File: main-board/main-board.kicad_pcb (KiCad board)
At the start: 2 copper layers, 62 parts, among them J1 MOTOR0, J10 PROGRAMMER, J11 CAM0, J12 CAM1, J13 CAM2, J14 CAM3, J15 CAM4, J16 CAM5, J17 CAM6, J18 CAM7, J19 PowerBoard Interface, J2 MOTOR1, J20 IMU Breakout, J21 ICSP (DO NOT POPULATE), J3 MOTOR2, J4 MOTOR3, J5 RJ45, J6 MOTOR4, J7 MOTOR5, J8 MOTOR6, J9 MOTOR7, SW1 SW_SPST, T1 ATB2012E-50011M-T01, T2 ATB2012E-50011M-T01, U1 MCP2515-EST, U2 ATA6560, U3 ATmega2560-16AU | Main Proc, U4 MC14051B, U5 MC14051B, U6 SN75HVD3082EDR, U7 LTC1983ES6-5-TRPBF, U8 OPAMP, U9 OPAMP, Y1 20MHz, Y2 20MHz

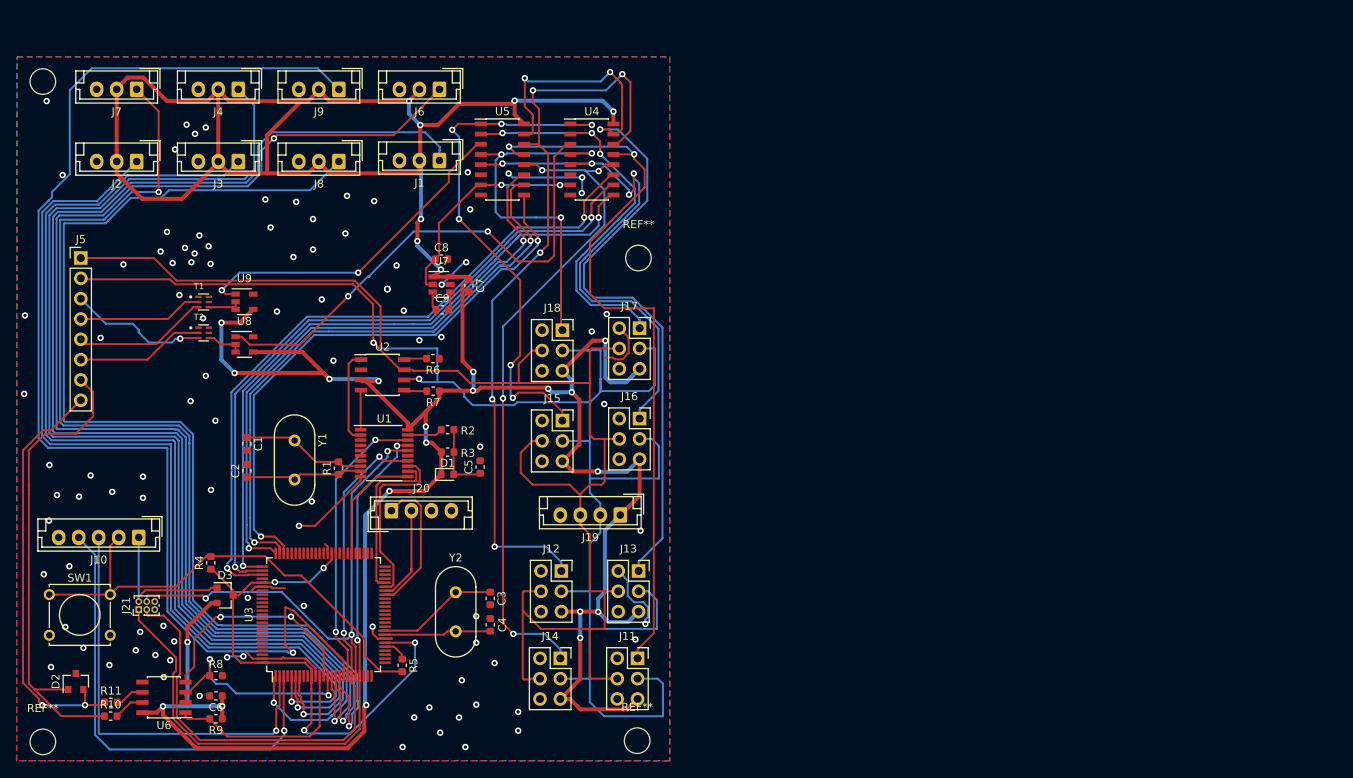
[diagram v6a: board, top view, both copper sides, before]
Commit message: Various changes (see description)
Schematic Changes:
* add optional second RS485
* add filter caps to IC power
* remove input resistor on reset line of 2560
* change CAN UART lines to be tx<>tx rx<>rx

PCB Changes:
* reorganize camera section
* add header labels
* minor fixes
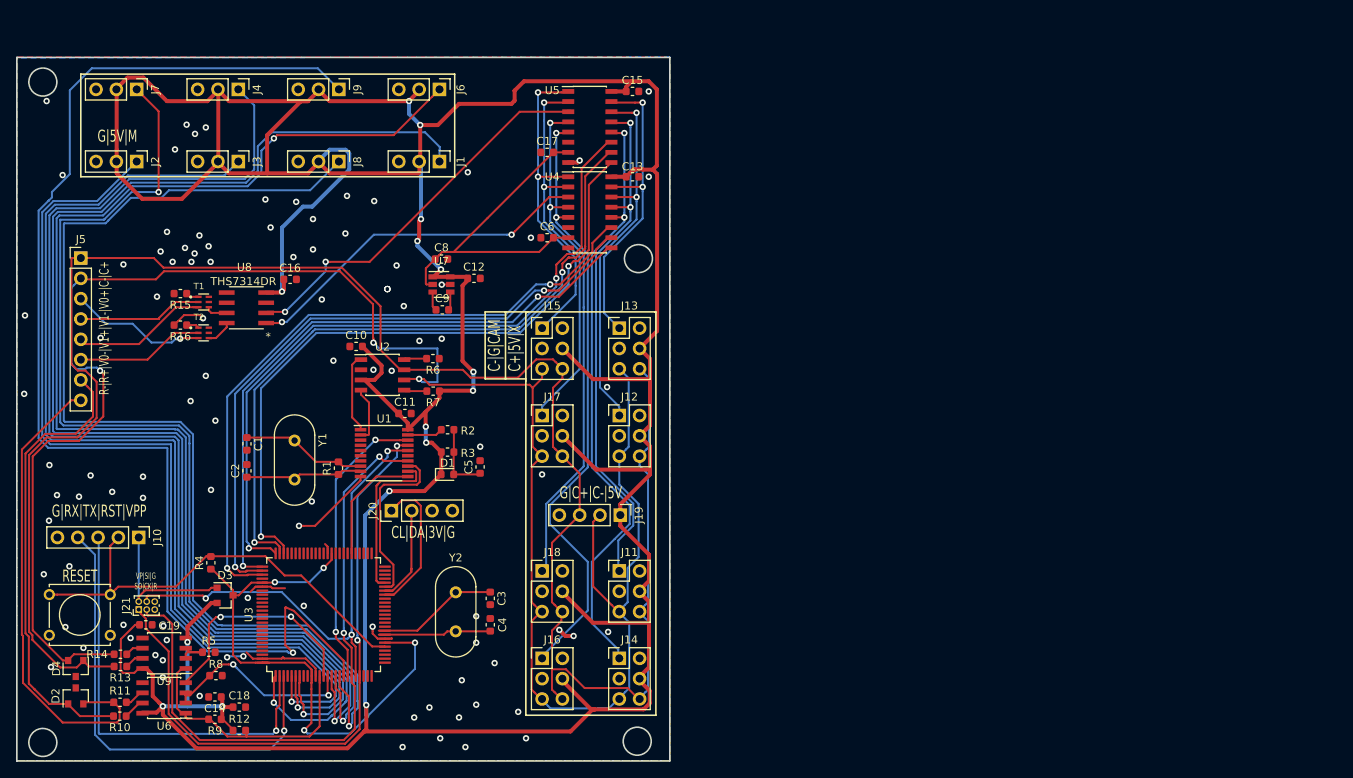
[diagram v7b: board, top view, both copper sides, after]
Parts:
- removed C7: 10uF, Capacitor_SMD:C_0603_1608Metric
- removed REF** (x4): MountingHole_3.2mm_M3, MountingHole:MountingHole_3.2mm_M3
- added C10: 100nF, Capacitor_SMD:C_0603_1608Metric, F.Cu at (107.4, 77.5)
- added C11: 100nF, Capacitor_SMD:C_0603_1608Metric, F.Cu at (113.5, 85.9)
- added C12: 100nF, Capacitor_SMD:C_0603_1608Metric, F.Cu at (122.2, 69.0)
- added C13: 100nF, Capacitor_SMD:C_0603_1608Metric, F.Cu at (142.0, 56.3)
- added C14: 100nF, Capacitor_SMD:C_0603_1608Metric, F.Cu at (89.8, 121.3)
- added C15: 100nF, Capacitor_SMD:C_0603_1608Metric, F.Cu at (142.0, 45.6)
- added C16: 100nF, Capacitor_SMD:C_0603_1608Metric, F.Cu at (99.2, 69.1)
- added C17: 100nF, Capacitor_SMD:C_0603_1608Metric, F.Cu at (131.3, 53.2)
- added C18: 100nF, Capacitor_SMD:C_0603_1608Metric, F.Cu at (92.8, 122.6)
- added C19: 100nF, Capacitor_SMD:C_0603_1608Metric, F.Cu at (81.2, 112.3)
- added D4: CDSOT23-SM712, Package_TO_SOT_SMD:SOT-23, F.Cu at (72.4, 117.7)
- added R12: 10k, Resistor_SMD:R_0603_1608Metric, F.Cu at (92.8, 125.5)
- added R13: 10, Resistor_SMD:R_0603_1608Metric, F.Cu at (78.0, 117.5)
- added R14: 10, Resistor_SMD:R_0603_1608Metric, F.Cu at (78.0, 116.0)
- added R15: 100, Resistor_SMD:R_0603_1608Metric, F.Cu at (85.5, 70.9)
- added R16: 100, Resistor_SMD:R_0603_1608Metric, F.Cu at (85.5, 74.8)
- J1, J2, J3, J4, J6, J7, J8, J9: footprint Connector_JST:JST_EH_B03B-EH-A_1x03_P2.50mm_Vertical -> Connector_PinHeader_2.54mm:PinHeader_1x03_P2.54mm_Vertical
- J10: footprint Connector_JST:JST_EH_B05B-EH-A_1x05_P2.50mm_Vertical -> Connector_PinHeader_2.54mm:PinHeader_1x05_P2.54mm_Vertical
- J11, J12, J13, J14, J15, J16, J17, J18: footprint Connector_PinSocket_2.54mm:PinSocket_2x03_P2.54mm_Vertical -> Connector_PinHeader_2.54mm:PinHeader_2x03_P2.54mm_Vertical
- J19, J20: footprint Connector_JST:JST_EH_B04B-EH-A_1x04_P2.50mm_Vertical -> Connector_PinHeader_2.54mm:PinHeader_1x04_P2.54mm_Vertical
- R5: value 100k -> 10k
- U8: value OPAMP -> THS7314DR; footprint Package_TO_SOT_SMD:SOT-23-5 -> ths7314dr:THS7314DR
- U9: value OPAMP -> SN75HVD3082EDR; footprint Package_TO_SOT_SMD:SOT-23-5 -> Package_SO:SOIC-8_3.9x4.9mm_P1.27mm
- moved C6 70.7 mm to (131.3, 63.9)
- moved U9 45.1 mm to (83.4, 115.8), turned to 180 degrees
- moved J16 32.4 mm to (130.7, 116.5)
- moved J13 30.4 mm to (140.3, 75.2)
- moved J18 30.2 mm to (130.7, 105.5)
- moved R5 24.2 mm to (89.0, 115.7), turned to 0 degrees
- moved J12 20.7 mm to (140.3, 86.1)
- moved J17 16.4 mm to (130.7, 86.1)
- moved J15 11.8 mm to (130.7, 75.2)
- moved U5 11.7 mm to (136.7, 50.0)
- moved J11 11.2 mm to (140.3, 105.5)
- moved J14 7.37 mm to (140.3, 116.5)
- moved U4 6.61 mm to (136.7, 60.7)
- moved U8 4.58 mm to (93.7, 72.6), turned to 180 degrees
- moved D2 1.81 mm to (72.4, 121.2)
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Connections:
- C6 pad 1: +5V -> -5V
- D3 pad 3: Net-(D3-Pad3) -> +5V
- J11 pad 2: GND -> Net-(J11-Pad2)
- J11 pad 3: CAN- -> GND
- J11 pad 4: CAN+ -> +5V
- J11 pad 5: +5V -> CAN-
- J11 pad 6: Net-(J11-Pad6) -> CAN+
- J12 pad 2: GND -> Net-(J12-Pad2)
- J12 pad 3: CAN- -> GND
- J12 pad 4: CAN+ -> +5V
- J12 pad 5: +5V -> CAN-
- J12 pad 6: Net-(J12-Pad6) -> CAN+
- J13 pad 2: GND -> Net-(J13-Pad2)
- J13 pad 3: CAN- -> GND
- J13 pad 4: CAN+ -> +5V
- J13 pad 5: +5V -> CAN-
- J13 pad 6: Net-(J13-Pad6) -> CAN+
- J14 pad 2: GND -> Net-(J14-Pad2)
- J14 pad 3: CAN- -> GND
- J14 pad 4: CAN+ -> +5V
- J14 pad 5: +5V -> CAN-
- J14 pad 6: Net-(J14-Pad6) -> CAN+
- J15 pad 2: GND -> Net-(J15-Pad2)
- J15 pad 3: CAN- -> GND
- J15 pad 4: CAN+ -> +5V
- J15 pad 5: +5V -> CAN-
- J15 pad 6: Net-(J15-Pad6) -> CAN+
- J16 pad 2: GND -> Net-(J16-Pad2)
- J16 pad 3: CAN- -> GND
- J16 pad 4: CAN+ -> +5V
- J16 pad 5: +5V -> CAN-
- J16 pad 6: Net-(J16-Pad6) -> CAN+
- J17 pad 2: GND -> Net-(J17-Pad2)
- J17 pad 3: CAN- -> GND
- J17 pad 4: CAN+ -> +5V
- J17 pad 5: +5V -> CAN-
- J17 pad 6: Net-(J17-Pad6) -> CAN+
- J18 pad 2: GND -> Net-(J18-Pad2)
- J18 pad 3: CAN- -> GND
- J18 pad 4: CAN+ -> +5V
- J18 pad 5: +5V -> CAN-
- J18 pad 6: Net-(J18-Pad6) -> CAN+
- R4 pad 1: Net-(D3-Pad3) -> +5V
- R5 pad 2: RESET-MAIN -> GND
- T1 pad 1: GND -> Net-(R15-Pad1)
- T2 pad 1: GND -> Net-(R16-Pad1)
- U2 pad 1: Net-(U1-Pad2) -> Net-(U1-Pad1)
- U2 pad 4: Net-(U1-Pad1) -> Net-(U1-Pad2)
- U3 pad 10: Net-(D3-Pad3) -> +5V
- U3 pad 100: Net-(D3-Pad3) -> +5V
- U3 pad 30: Net-(R5-Pad1) -> RESET-MAIN
- U3 pad 31: Net-(D3-Pad3) -> +5V
- U3 pad 61: Net-(D3-Pad3) -> +5V
- U3 pad 80: Net-(D3-Pad3) -> +5V
- U8 pad 2: Net-(T2-Pad4) -> VID-CAM1
- U8 pad 3: Net-(T2-Pad4) -> Net-(U8-Pad3)
- U9 pad 1: VID-CAM1 -> RS485-R
- U9 pad 2: Net-(T1-Pad4) -> Net-(R5-Pad1)
- U9 pad 3: Net-(T1-Pad4) -> Net-(R5-Pad1)
- U9 pad 4: +5V -> Net-(U9-Pad4)
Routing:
- net +5V: track 469.8 -> 624.8 mm, vias 27 -> 19
- net Net-(D3-Pad3): track 71.2 -> 0.00 mm, vias 4 -> 0
- net CAN+: track 178.2 -> 242.6 mm
- net CAM2: track 101.1 -> 38.8 mm, vias 3 -> 2
- net CAN-: track 204.4 -> 255.1 mm, vias 2 -> 3
- net CAM1: track 95.3 -> 47.0 mm, vias 5 -> 2
- net CAM0: track 95.1 -> 65.3 mm
- net CAM4: track 66.8 -> 40.8 mm, vias 6 -> 2
- net GND: track 67.7 -> 43.6 mm, vias 100 -> 98
- net VID-CAM0: track 63.0 -> 44.3 mm
- net CAM7: track 46.8 -> 64.8 mm, vias 3 -> 2
- net -5V: track 28.0 -> 42.1 mm, vias 2 -> 0
- net VID1-0: track 76.8 -> 89.1 mm
- net VID1-2: track 72.7 -> 84.4 mm
- net VID1-1: track 76.2 -> 87.3 mm
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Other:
- board outline added: 81.6 x 87.9 mm
- board text added: "C+|5V|X"
- board text added: "C-|G|CAM"
- board text added: "CL|DA|3V|G"
- board text added: "G|5V|M"
- board text added: "G|C+|C-|5V"
- board text added: "G|RX|TX|RST|VPP"
- board text added: "MISSOURI S&T UNDERWATER ROBOTICS TEAM MAIN BOARD | PCB 1.0.0 | SCH 1.0.0 MATTHEW (COOPER) HEALY, MICHAELA DICKERSON"
- board text added: "R-|R+|V0-|V1+|V1-|V0+|C-|C+"
- board text added: "RESET"
- board text added: "VP|SI|G SO|CK|R"

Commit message: S1.0.1 B1.0.1 See Desc
* Reorganized video and motor connectors for easier ROV wiring

* PCB Via redesign
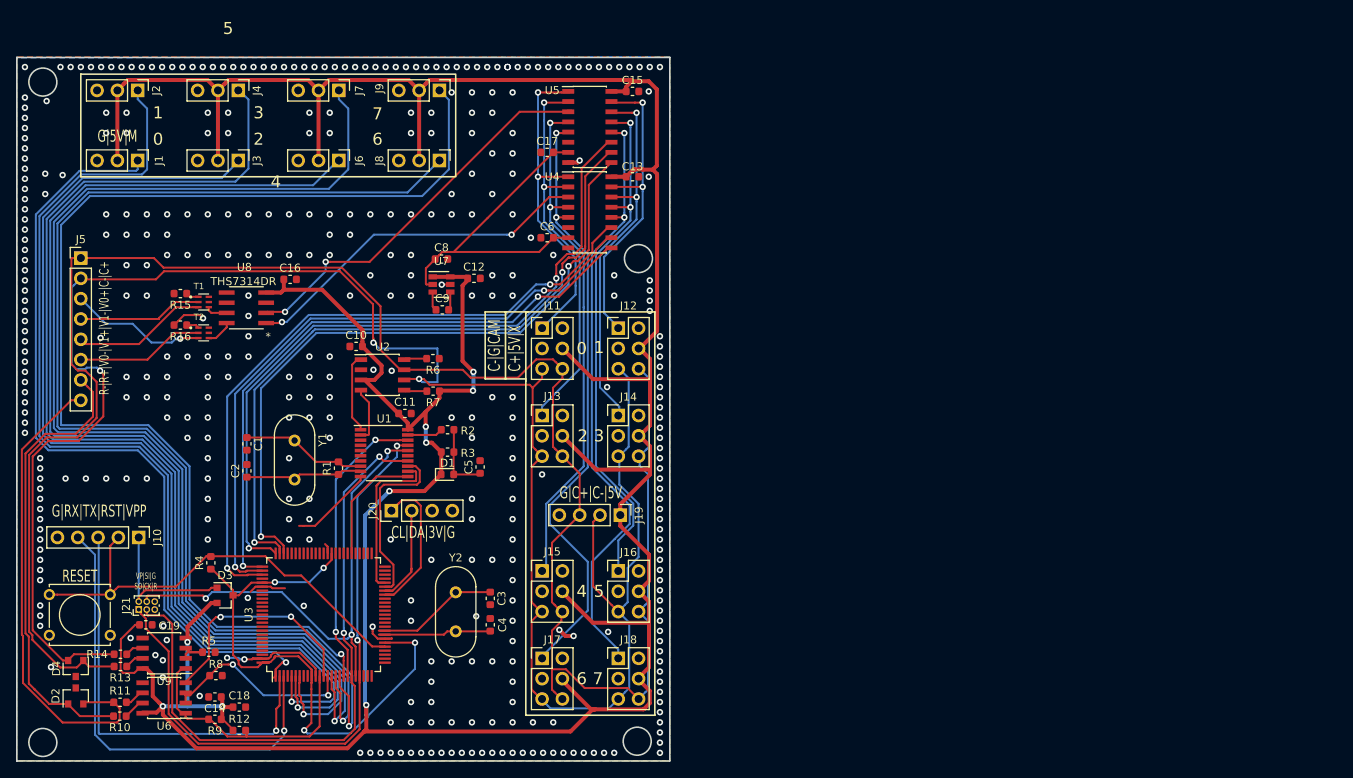
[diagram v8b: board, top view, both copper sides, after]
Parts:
- moved J1 37.7 mm to (80.1, 54.2)
- moved J11 31.9 mm to (130.7, 75.2)
- moved J14 30.4 mm to (140.2, 86.1)
- moved J15 30.4 mm to (130.7, 105.5)
- moved J17 30.4 mm to (130.7, 116.5)
- moved J7 25.3 mm to (105.3, 45.5)
- moved J6 15.4 mm to (105.3, 54.2)
- moved J13 14.6 mm to (130.7, 86.1)
- moved J16 14.5 mm to (140.2, 105.5)
- moved J18 14.5 mm to (140.2, 116.5)
- moved J8 12.6 mm to (117.9, 54.2)
- moved J9 12.6 mm to (117.9, 45.5)
- moved J12 10.9 mm to (140.2, 75.2)
- moved J2 8.89 mm to (80.1, 45.5)
- moved J3 0.13 mm to (92.7, 54.2)
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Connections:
- U4 pad 1: CAM4 -> CAM0
- U4 pad 12: CAM3 -> CAM7
- U4 pad 13: CAM0 -> CAM5
- U4 pad 14: CAM1 -> CAM3
- U4 pad 15: CAM2 -> CAM1
- U4 pad 2: CAM6 -> CAM2
- U4 pad 4: CAM7 -> CAM4
- U4 pad 5: CAM5 -> CAM6
- U5 pad 1: CAM4 -> CAM0
- U5 pad 12: CAM3 -> CAM7
- U5 pad 13: CAM0 -> CAM5
- U5 pad 14: CAM1 -> CAM3
- U5 pad 15: CAM2 -> CAM1
- U5 pad 2: CAM6 -> CAM2
- U5 pad 4: CAM7 -> CAM4
- U5 pad 5: CAM5 -> CAM6
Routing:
- net +5V: track 624.8 -> 544.7 mm, vias 19 -> 13
- net M0: track 162.6 -> 99.5 mm
- net CAM3: track 75.9 -> 47.0 mm
- net CAM6: track 49.1 -> 76.9 mm
- net CAM0: track 65.3 -> 40.8 mm
- net CAM4: track 40.8 -> 64.8 mm
- net M4: track 156.2 -> 136.6 mm, vias 2 -> 1
- net M5: track 127.5 -> 146.9 mm, vias 2 -> 1
- net CAM5: track 76.9 -> 65.3 mm
- net M6: track 137.9 -> 149.1 mm
- net CAM7: track 64.8 -> 75.9 mm
- net CAM2: track 38.8 -> 49.1 mm
- net M1: track 114.6 -> 123.7 mm
- net CAM1: track 47.0 -> 38.8 mm
- net M7: track 154.6 -> 147.2 mm
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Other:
- board text added: "0"
- board text added: "1"
- board text added: "2"
- board text added: "3"
- board text added: "4"
- board text added: "5"
- board text added: "6"
- board text added: "7"
- board text added: "MISSOURI S&T UNDERWATER ROBOTICS TEAM MAIN BOARD | PCB 1.0.1 | SCH 1.0.1 MATTHEW (COOPER) HEALY, MICHAELA DICKERSON"
- board text removed: "MISSOURI S&T UNDERWATER ROBOTICS TEAM MAIN BOARD | PCB 1.0.0 | SCH 1.0.0 MATTHEW (COOPER) HEALY, MICHAELA DICKERSON"
